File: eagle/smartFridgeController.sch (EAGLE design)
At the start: 7 parts

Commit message: might work
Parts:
- removed CPC1709: (no value), SparkFun-Connectors:CONN_05
- added CPC1706: S102S02, relay:S102S02
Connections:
- net +VE: now also CPC1706.DS1, JST.1; no longer CPC1709.4
- net -VE: now also CPC1706.DS2, JST.2; no longer CPC1709.5
- net D8_RELAY_PIN: now also CPC1706.K; no longer CPC1709.1
- net GND: now also CPC1706.A; no longer CPC1709.2
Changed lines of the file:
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@@
 <part name="SUPPLY3" library="supply2" deviceset="GND" device=""/>
 <part name="OKI-78SR-5/1.5-W36-C" library="SparkFun-Connectors" deviceset="CONN_03" device="" value="Regulator"/>
-<part name="CPC1709" library="SparkFun-Connectors" deviceset="CONN_05" device=""/>
+<part name="CPC1706" library="relay" library_urn="urn:adsk.eagle:library:339" deviceset="S*02S02" device="" package3d_urn="urn:adsk.eagle:package:24541/1" technology="1"/>
 </parts>
 <sheets>
@@
 <instance part="SUPPLY3" gate="GND" x="124.46" y="73.66"/>
 <instance part="OKI-78SR-5/1.5-W36-C" gate="J$1" x="238.76" y="55.88" rot="R180"/>
-<instance part="CPC1709" gate="G$1" x="43.18" y="149.86"/>
+<instance part="CPC1706" gate="G$1" x="93.98" y="149.86"/>
 </instances>
 <busses>
@@
 </segment>
 <segment>
-<pinref part="CPC1709" gate="G$1" pin="2"/>
-<wire x1="50.8" y1="147.32" x2="58.42" y2="147.32" width="0.1524" layer="91"/>
-<label x="50.8" y="147.32" size="1.778" layer="95"/>
+<pinref part="CPC1706" gate="G$1" pin="A"/>
+<wire x1="83.82" y1="152.4" x2="66.04" y2="152.4" width="0.1524" layer="91"/>
+<label x="66.04" y="152.4" size="1.778" layer="95"/>
 </segment>
 </net>
@@
 </segment>
 </net>
-<net name="A0_VCC_VD" class="0">
+<net name="A0_VCC_VD" class="1">
 <segment>
 <pinref part="U$1" gate="G$1" pin="A0"/>
@@
 </segment>
 </net>
-<net name="D8_RELAY_PIN" class="0">
-<segment>
-<pinref part="CPC1709" gate="G$1" pin="1"/>
-<wire x1="50.8" y1="144.78" x2="58.42" y2="144.78" width="0.1524" layer="91"/>
-<label x="50.8" y="144.78" size="1.778" layer="95"/>
-</segment>
+<net name="D8_RELAY_PIN" class="1">
 <segment>
 <pinref part="U$1" gate="G$1" pin="D8"/>
@@
 <label x="48.26" y="58.42" size="1.778" layer="95"/>
 </segment>
-</net>
-<net name="+VE" class="0">
 <segment>
-<pinref part="CPC1709" gate="G$1" pin="4"/>
-<wire x1="50.8" y1="152.4" x2="58.42" y2="152.4" width="0.1524" layer="91"/>
-<label x="50.8" y="152.4" size="1.778" layer="95"/>
+<pinref part="CPC1706" gate="G$1" pin="K"/>
+<wire x1="83.82" y1="147.32" x2="66.04" y2="147.32" width="0.1524" layer="91"/>
+<label x="66.04" y="147.32" size="1.778" layer="95"/>
 </segment>
 </net>
-<net name="-VE" class="0">
+<net name="+VE" class="1">
 <segment>
-<pinref part="CPC1709" gate="G$1" pin="5"/>
-<wire x1="50.8" y1="154.94" x2="58.42" y2="154.94" width="0.1524" layer="91"/>
-<label x="50.8" y="154.94" size="1.778" layer="95"/>
+<pinref part="JST" gate="G$1" pin="1"/>
+<wire x1="144.78" y1="40.64" x2="154.94" y2="40.64" width="0.1524" layer="91"/>
+<label x="144.78" y="40.64" size="1.778" layer="95"/>
+</segment>
+<segment>
+<pinref part="CPC1706" gate="G$1" pin="DS1"/>
+<wire x1="104.14" y1="152.4" x2="116.84" y2="152.4" width="0.1524" layer="91"/>
+<label x="106.68" y="152.4" size="1.778" layer="95"/>
+</segment>
+</net>
+<net name="-VE" class="1">
+<segment>
+<pinref part="JST" gate="G$1" pin="2"/>
+<wire x1="144.78" y1="43.18" x2="154.94" y2="43.18" width="0.1524" layer="91"/>
+<label x="144.78" y="43.18" size="1.778" layer="95"/>
+</segment>
+<segment>
+<pinref part="CPC1706" gate="G$1" pin="DS2"/>
+<wire x1="104.14" y1="147.32" x2="116.84" y2="147.32" width="0.1524" layer="91"/>
+<label x="106.68" y="147.32" size="1.778" layer="95"/>
 </segment>
 </net>
@@
 </schematic>
 </drawing>
+<compatibility>
+<note version="8.2" severity="warning">
+Since Version 8.2, EAGLE supports online libraries. The ids
+of those online libraries will not be understood (or retained)
+with this version.
+</note>
+<note version="8.3" severity="warning">
+Since Version 8.3, EAGLE supports URNs for individual library
+assets (packages, symbols, and devices). The URNs of those assets
+will not be understood (or retained) with this version.
+</note>
+<note version="8.3" severity="warning">
+Since Version 8.3, EAGLE supports the association of 3D packages
+with devices in libraries, schematics, and board files. Those 3D
+packages will not be understood (or retained) with this version.
+</note>
+</compatibility>
 </eagle>

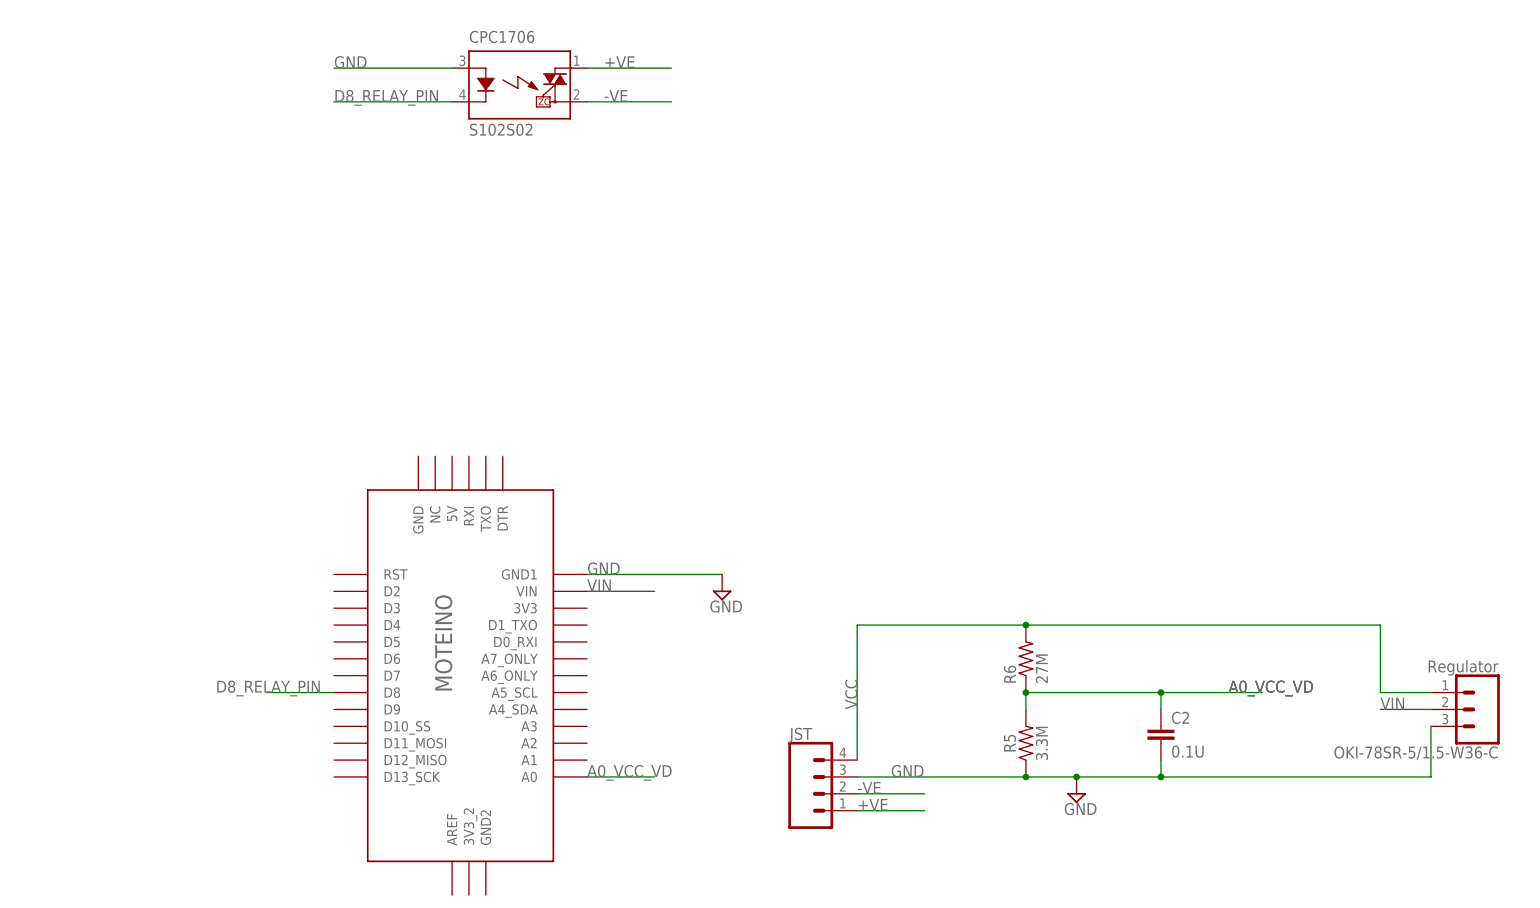
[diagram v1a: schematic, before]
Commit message: Added DS header
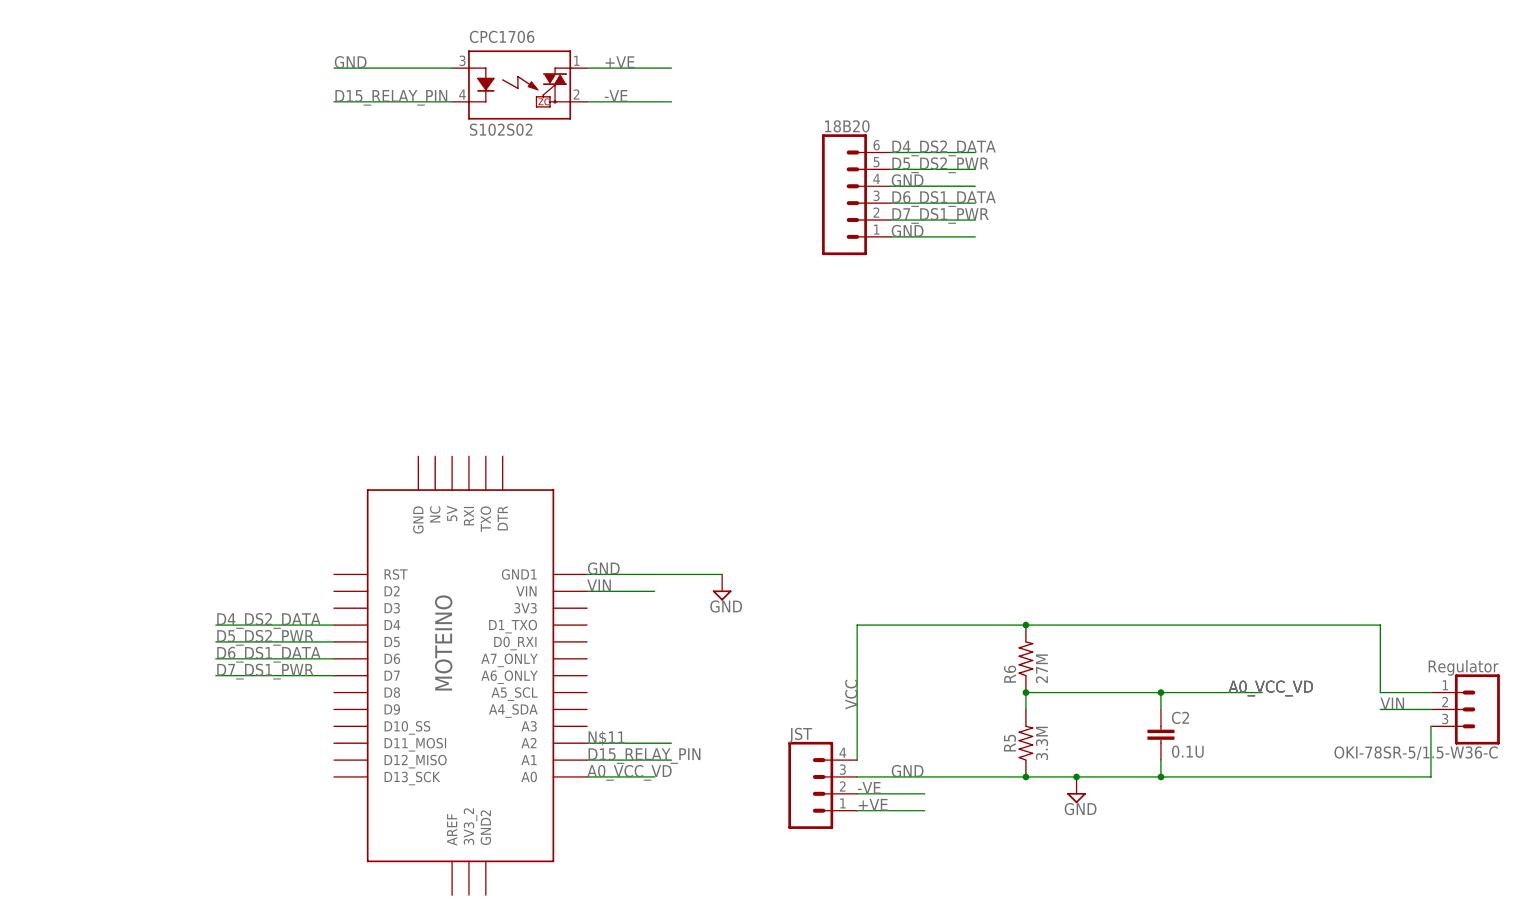
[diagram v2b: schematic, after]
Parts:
- added 18B20: (no value), SparkFun-Connectors:CONN_06SILK_FEMALE_PTH
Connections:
- removed net D8_RELAY_PIN: CPC1706.K, U$1.D8
- new net D15_RELAY_PIN: CPC1706.K, U$1.A1
- new net D4_DS2_DATA: 18B20.6, U$1.D4
- new net D5_DS2_PWR: 18B20.5, U$1.D5
- new net D6_DS1_DATA: 18B20.3, U$1.D6
- new net D7_DS1_PWR: 18B20.2, U$1.D7
- new net N$11: U$1.A2
- net GND: now also 18B20.1, 18B20.4
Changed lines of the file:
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@@
 <part name="OKI-78SR-5/1.5-W36-C" library="SparkFun-Connectors" deviceset="CONN_03" device="" value="Regulator"/>
 <part name="CPC1706" library="relay" library_urn="urn:adsk.eagle:library:339" deviceset="S*02S02" device="" package3d_urn="urn:adsk.eagle:package:24541/1" technology="1"/>
+<part name="18B20" library="SparkFun-Connectors" deviceset="CONN_06" device="SILK_FEMALE_PTH"/>
 </parts>
 <sheets>
@@
 <instance part="OKI-78SR-5/1.5-W36-C" gate="J$1" x="238.76" y="55.88" rot="R180"/>
 <instance part="CPC1706" gate="G$1" x="93.98" y="149.86"/>
+<instance part="18B20" gate="G$1" x="144.78" y="132.08"/>
 </instances>
 <busses>
@@
 <wire x1="83.82" y1="152.4" x2="66.04" y2="152.4" width="0.1524" layer="91"/>
 <label x="66.04" y="152.4" size="1.778" layer="95"/>
+</segment>
+<segment>
+<pinref part="18B20" gate="G$1" pin="4"/>
+<wire x1="149.86" y1="134.62" x2="162.56" y2="134.62" width="0.1524" layer="91"/>
+<label x="149.86" y="134.62" size="1.778" layer="95"/>
+</segment>
+<segment>
+<pinref part="18B20" gate="G$1" pin="1"/>
+<wire x1="149.86" y1="127" x2="162.56" y2="127" width="0.1524" layer="91"/>
+<label x="149.86" y="127" size="1.778" layer="95"/>
 </segment>
 </net>
@@
 </segment>
 </net>
-<net name="D8_RELAY_PIN" class="1">
-<segment>
-<pinref part="U$1" gate="G$1" pin="D8"/>
-<wire x1="66.04" y1="58.42" x2="55.88" y2="58.42" width="0.1524" layer="91"/>
-<label x="48.26" y="58.42" size="1.778" layer="95"/>
-</segment>
-<segment>
-<pinref part="CPC1706" gate="G$1" pin="K"/>
-<wire x1="83.82" y1="147.32" x2="66.04" y2="147.32" width="0.1524" layer="91"/>
-<label x="66.04" y="147.32" size="1.778" layer="95"/>
-</segment>
-</net>
 <net name="+VE" class="1">
 <segment>
@@
 </segment>
 </net>
+<net name="D7_DS1_PWR" class="0">
+<segment>
+<pinref part="U$1" gate="G$1" pin="D7"/>
+<wire x1="66.04" y1="60.96" x2="48.26" y2="60.96" width="0.1524" layer="91"/>
+<label x="48.26" y="60.96" size="1.778" layer="95"/>
+</segment>
+<segment>
+<pinref part="18B20" gate="G$1" pin="2"/>
+<wire x1="149.86" y1="129.54" x2="162.56" y2="129.54" width="0.1524" layer="91"/>
+<label x="149.86" y="129.54" size="1.778" layer="95"/>
+</segment>
+</net>
+<net name="D6_DS1_DATA" class="0">
+<segment>
+<pinref part="U$1" gate="G$1" pin="D6"/>
+<wire x1="66.04" y1="63.5" x2="48.26" y2="63.5" width="0.1524" layer="91"/>
+<label x="48.26" y="63.5" size="1.778" layer="95"/>
+</segment>
+<segment>
+<pinref part="18B20" gate="G$1" pin="3"/>
+<wire x1="149.86" y1="132.08" x2="162.56" y2="132.08" width="0.1524" layer="91"/>
+<label x="149.86" y="132.08" size="1.778" layer="95"/>
+</segment>
+</net>
+<net name="D4_DS2_DATA" class="0">
+<segment>
+<pinref part="U$1" gate="G$1" pin="D4"/>
+<wire x1="66.04" y1="68.58" x2="48.26" y2="68.58" width="0.1524" layer="91"/>
+<label x="48.26" y="68.58" size="1.778" layer="95"/>
+</segment>
+<segment>
+<pinref part="18B20" gate="G$1" pin="6"/>
+<wire x1="149.86" y1="139.7" x2="162.56" y2="139.7" width="0.1524" layer="91"/>
+<label x="149.86" y="139.7" size="1.778" layer="95"/>
+</segment>
+</net>
+<net name="D15_RELAY_PIN" class="0">
+<segment>
+<pinref part="U$1" gate="G$1" pin="A1"/>
+<wire x1="104.14" y1="48.26" x2="116.84" y2="48.26" width="0.1524" layer="91"/>
+<label x="104.14" y="48.26" size="1.778" layer="95"/>
+</segment>
+<segment>
+<pinref part="CPC1706" gate="G$1" pin="K"/>
+<wire x1="83.82" y1="147.32" x2="66.04" y2="147.32" width="0.1524" layer="91"/>
+<label x="66.04" y="147.32" size="1.778" layer="95"/>
+</segment>
+</net>
+<net name="N$11" class="0">
+<segment>
+<pinref part="U$1" gate="G$1" pin="A2"/>
+<wire x1="104.14" y1="50.8" x2="116.84" y2="50.8" width="0.1524" layer="91"/>
+<label x="104.14" y="50.8" size="1.778" layer="95"/>
+</segment>
+</net>
+<net name="D5_DS2_PWR" class="0">
+<segment>
+<pinref part="U$1" gate="G$1" pin="D5"/>
+<wire x1="66.04" y1="66.04" x2="48.26" y2="66.04" width="0.1524" layer="91"/>
+<label x="48.26" y="66.04" size="1.778" layer="95"/>
+</segment>
+<segment>
+<pinref part="18B20" gate="G$1" pin="5"/>
+<wire x1="149.86" y1="137.16" x2="162.56" y2="137.16" width="0.1524" layer="91"/>
+<label x="149.86" y="137.16" size="1.778" layer="95"/>
+</segment>
+</net>

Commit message: extended board
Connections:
- removed net N$11: U$1.A2
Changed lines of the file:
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@@
-</segment>
-</net>
-<net name="N$11" class="0">
-<segment>
-<pinref part="U$1" gate="G$1" pin="A2"/>
-<wire x1="104.14" y1="50.8" x2="116.84" y2="50.8" width="0.1524" layer="91"/>
-<label x="104.14" y="50.8" size="1.778" layer="95"/>
 </segment>
 </net>

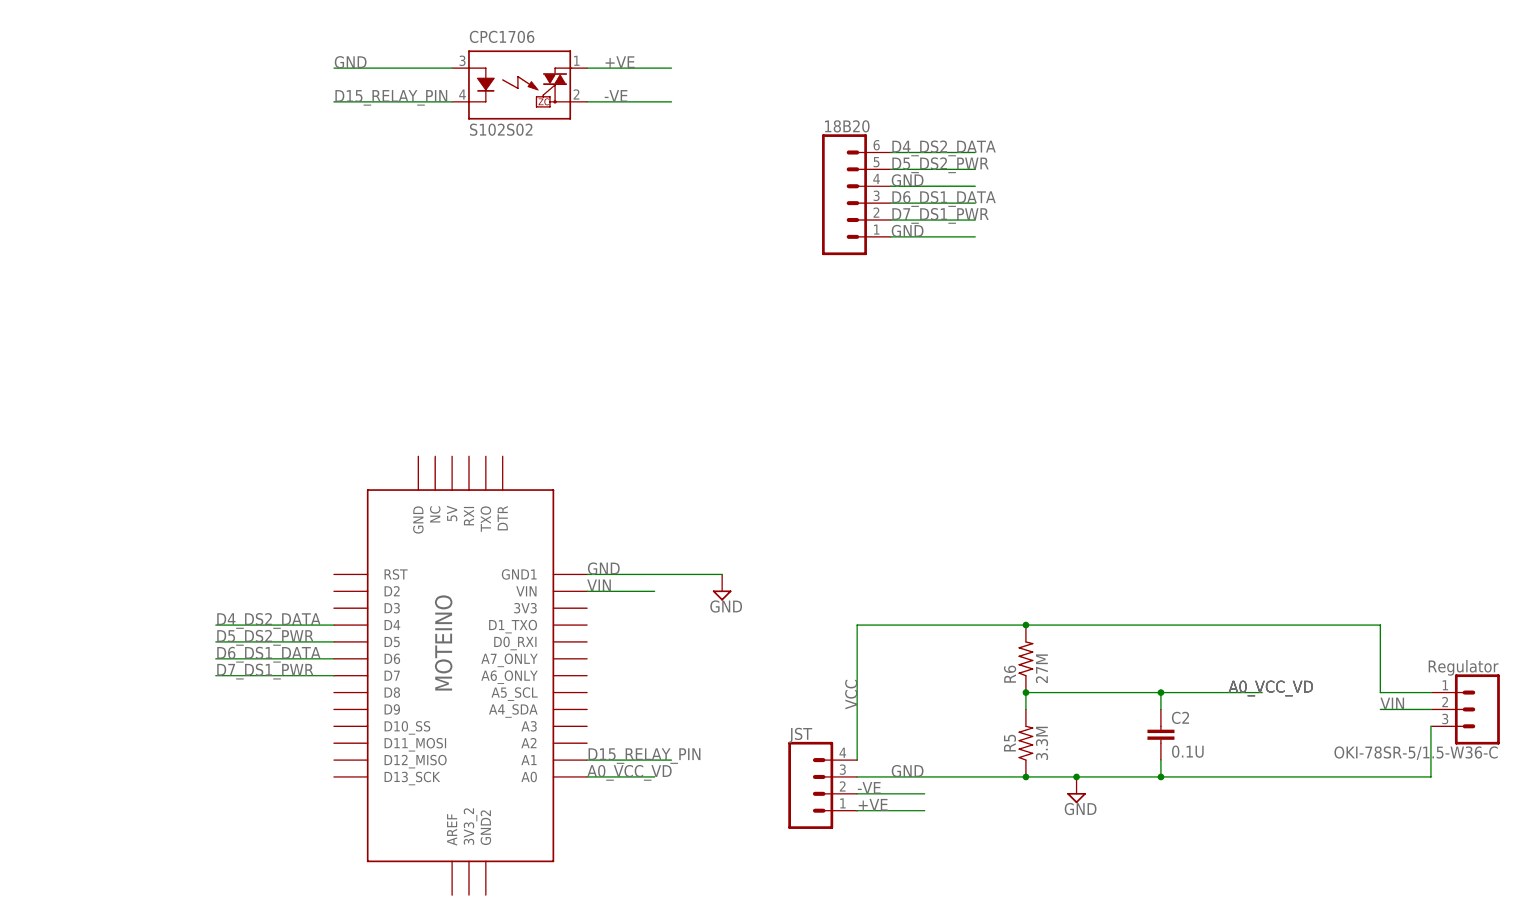
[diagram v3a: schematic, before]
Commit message: added 3 LEDs
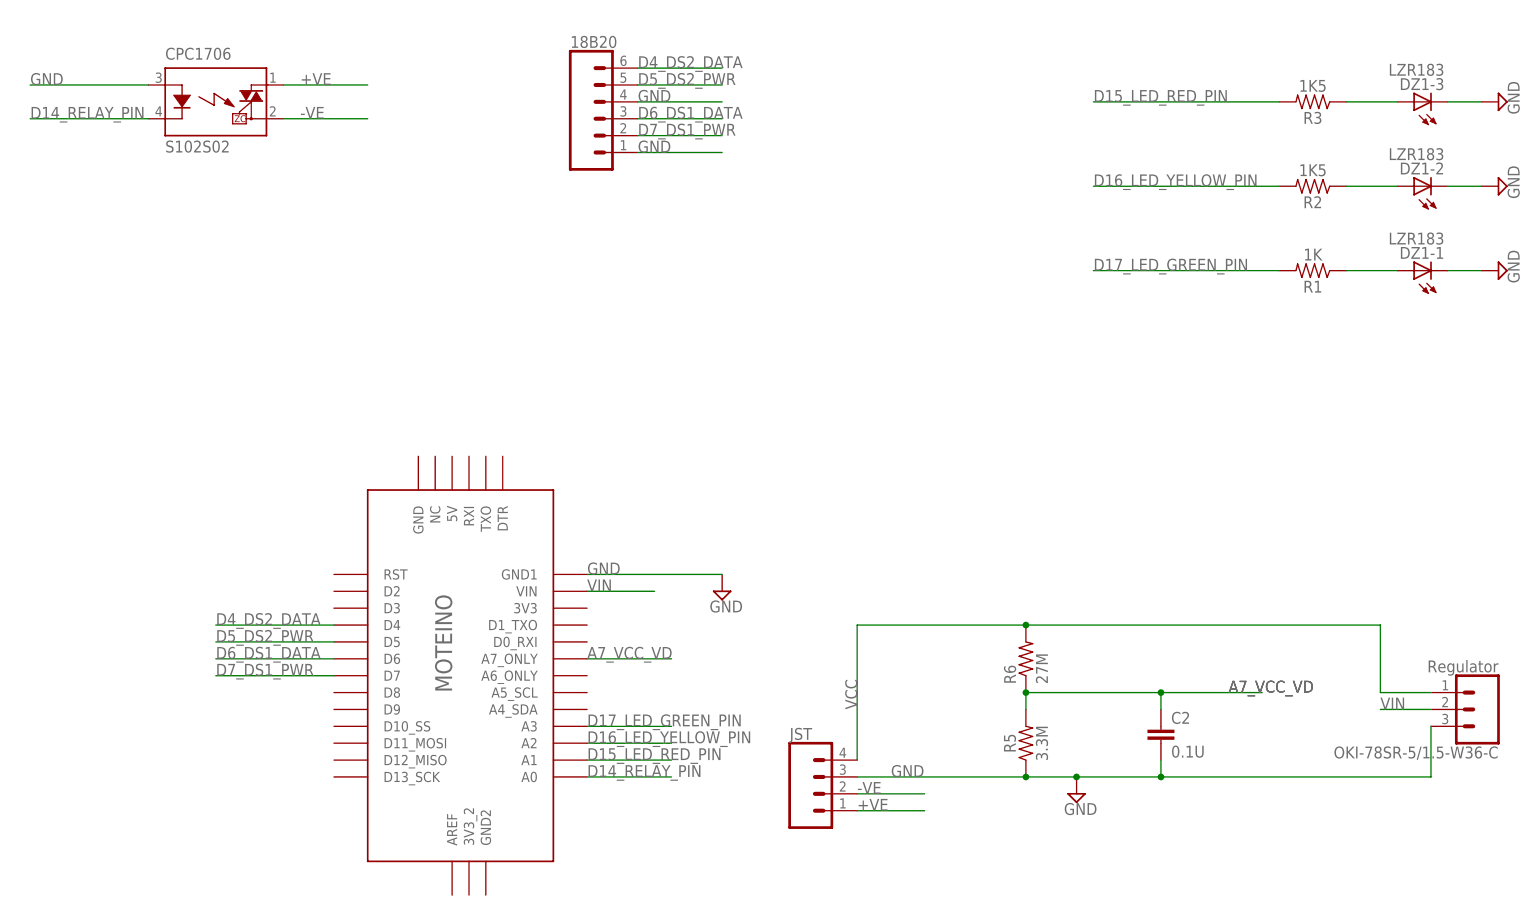
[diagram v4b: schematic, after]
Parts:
- added DZ1: LZR183, led:LZR183
- added R1: 1K, SparkFun-Resistors:1KOHM-HORIZ-1/4W-1%
- added R2, R3: 1K5, SparkFun-Resistors:1KOHM-HORIZ-1/4W-1%
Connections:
- removed net A0_VCC_VD: C2.1, R5.2, R6.1, U$1.A0
- removed net D15_RELAY_PIN: CPC1706.K, U$1.A1
- new net A7_VCC_VD: C2.1, R5.2, R6.1, U$1.A7_ONLY
- new net D14_RELAY_PIN: CPC1706.K, U$1.A0
- new net D15_LED_RED_PIN: R3.2, U$1.A1
- new net D16_LED_YELLOW_PIN: R2.2, U$1.A2
- new net D17_LED_GREEN_PIN: R1.2, U$1.A3
- new net N$1: DZ1-1.A, R1.1
- new net N$2: DZ1-2.A, R2.1
- new net N$3: DZ1-3.A, R3.1
- net GND: now also DZ1-1.C, DZ1-2.C, DZ1-3.C
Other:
- moved on the sheet: 18B20, CPC1706
